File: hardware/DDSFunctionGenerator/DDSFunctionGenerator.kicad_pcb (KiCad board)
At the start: 2 copper layers, 100 x 100 mm, 147 parts, among them J1 Conn_Coaxial, J2 USB_B_Micro, J3 Conn_Coaxial, J4 Conn_Coaxial, Q1 Q_NPN_BEC, Q2 Q_NPN_BEC, Q3 Q_NPN_BEC, Q4 BC859, Q5 BC848, Q6 Q_NPN_BEC, SW1 Rotary_Encoder_Switch, T1 Transformer_1P_1S, U1 TC1107-3.3VOA, U10 74HCT1G86, U2 L7805, U3 L7805, U4 AD9832, U5 STM32F030K6Tx, U6 FT200XD, U7 AD8325, U8 MCP3425A0T-ECH, U9 LM358, X1 XO91, Y1 Crystal

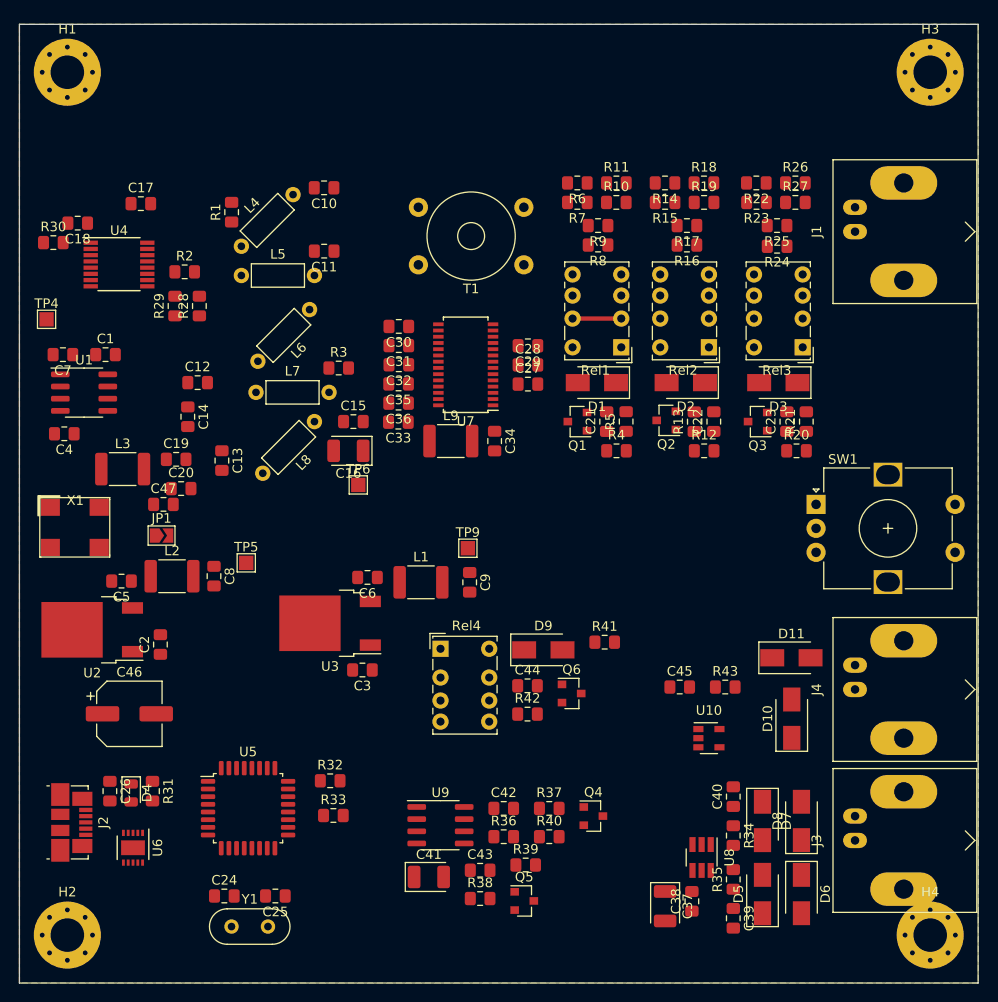
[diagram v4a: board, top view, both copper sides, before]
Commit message: added encoder 3d model
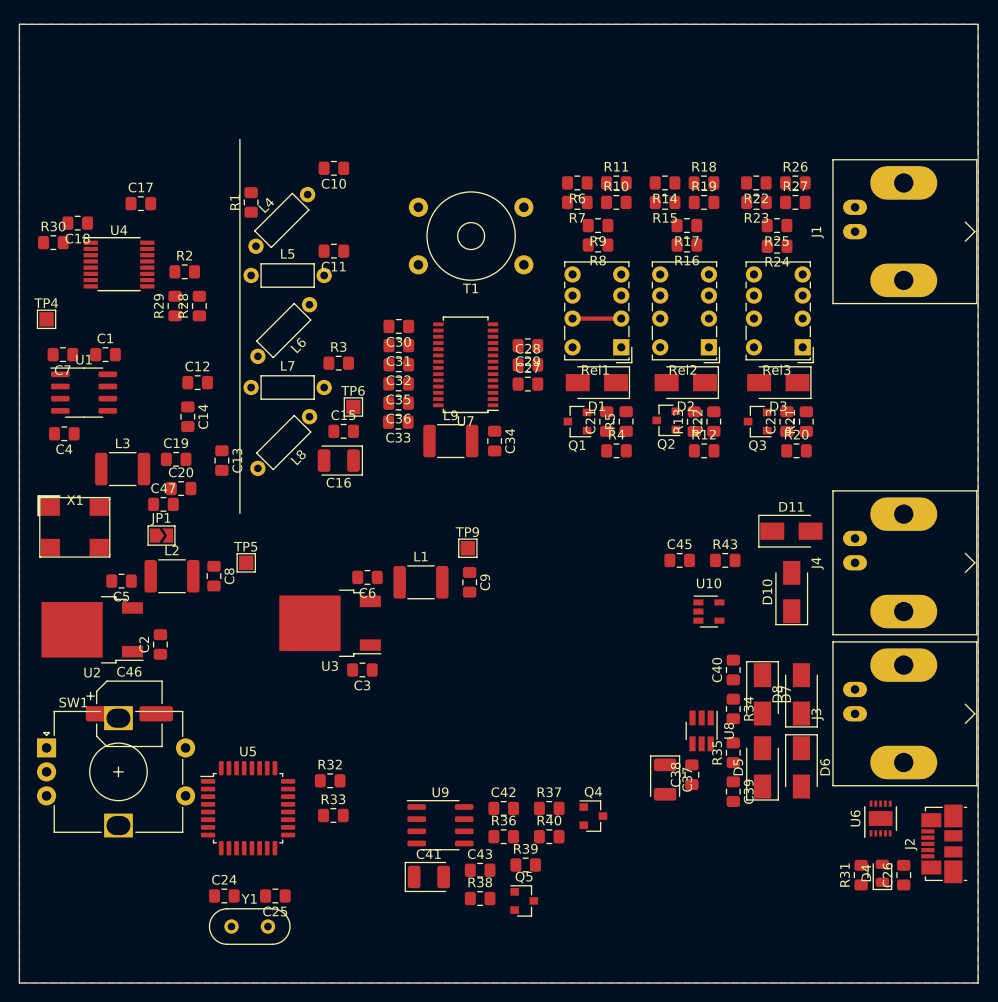
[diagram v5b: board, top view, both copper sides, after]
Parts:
- removed C44: 1n, Capacitor_SMD:C_0805_2012Metric_Pad1.15x1.40mm_HandSolder
- removed D9: D, Diode_SMD:D_SMA
- removed H1, H2, H3, H4: MountingHole_Pad, MountingHole:MountingHole_3.5mm_Pad_Via
- removed Q6: Q_NPN_BEC, Package_TO_SOT_SMD:SOT-23
- removed R41: 2k2, Resistor_SMD:R_0805_2012Metric_Pad1.15x1.40mm_HandSolder
- removed R42: 10k, Resistor_SMD:R_0805_2012Metric_Pad1.15x1.40mm_HandSolder
- removed Rel4: RSM850B-6112-85-1005, Relay_THT:Relay_DPDT_Omron_G6K-2P-Y
- moved J2 90.8 mm to (146.2, 135.5), turned to 90 degrees
- moved SW1 84.2 mm to (52.8, 125.5)
- moved C26 83.3 mm to (142.2, 138.7), turned to 90 degrees
- moved D4 78.8 mm to (140.0, 138.6), turned to 90 degrees
- moved U6 78.0 mm to (139.8, 132.8), turned to 90 degrees
- moved R31 74.4 mm to (137.8, 138.7), turned to 90 degrees
- moved C39 13.2 mm to (124.5, 130.0)
- moved C40 13.2 mm to (124.5, 117.3)
- moved D5 13.2 mm to (127.5, 127.5)
- moved D6 13.2 mm to (131.6, 127.5)
- moved R35 13.2 mm to (124.5, 126.0)
- moved U8 13.2 mm to (121.2, 123.7)
- moved C37 13.2 mm to (117.3, 128.8)
- moved C38 13.2 mm to (120.1, 128.3)
- moved C45 13.2 mm to (118.9, 105.9)
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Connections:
- R4 pad 2: REL_1 -> (no net)

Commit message: changed pcb size
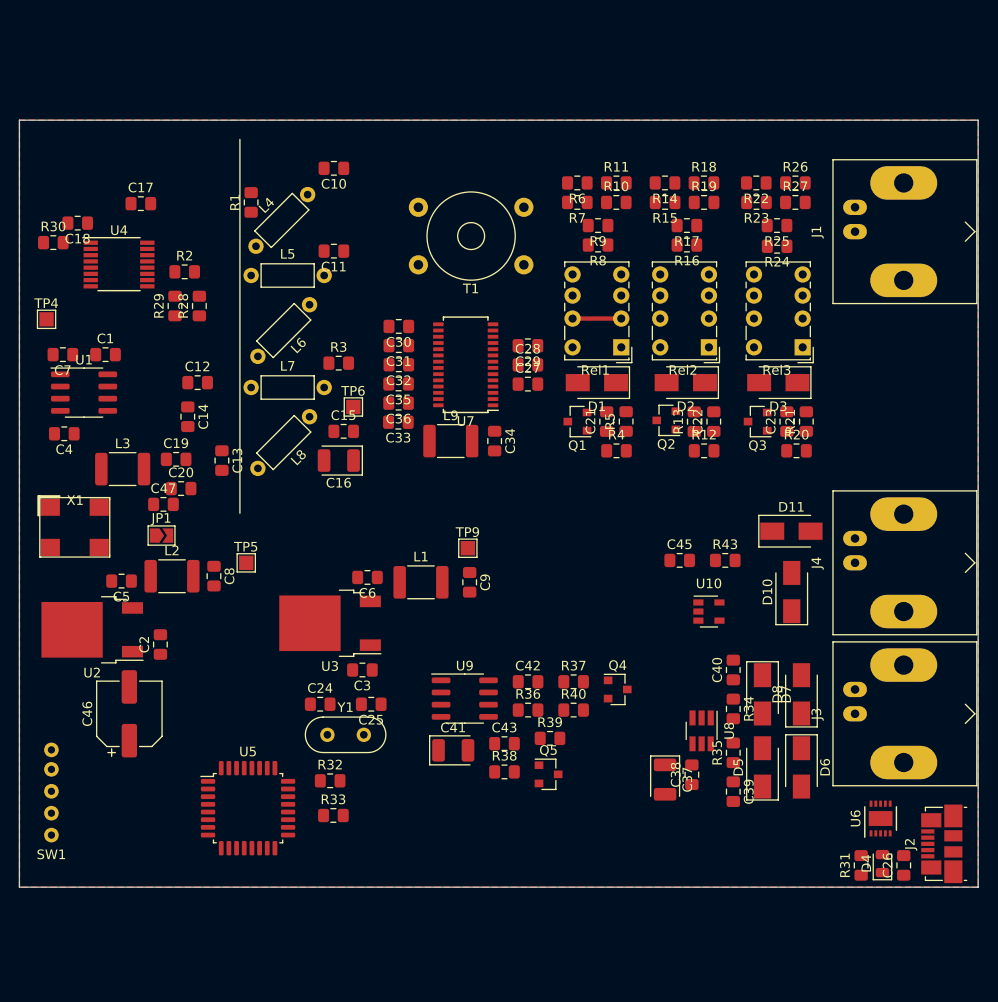
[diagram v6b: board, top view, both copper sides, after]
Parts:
- SW1: footprint Rotary_Encoder:RotaryEncoder_Alps_EC12E-Switch_Vertical_H20mm -> DDSFunctionGenerator:EN11-VNB1BQ15
- moved Y1 22.4 mm to (82.1, 124.1)
- moved C24 22.4 mm to (81.4, 120.9)
- moved C25 22.4 mm to (86.7, 120.9)
- moved C42 13.5 mm to (103.1, 118.6)
- moved R37 13.5 mm to (107.8, 118.6)
- moved U9 13.5 mm to (96.5, 120.3)
- moved Q4 13.5 mm to (112.4, 119.4)
- moved R36 13.5 mm to (103.1, 121.5)
- moved R40 13.5 mm to (107.8, 121.5)
- moved C43 13.5 mm to (100.6, 125.0)
- moved Q5 13.5 mm to (105.2, 128.2)
- moved C41 13.5 mm to (95.2, 125.7)
- moved R38 13.5 mm to (100.6, 128.0)
- moved R39 13.5 mm to (105.3, 124.5)
- moved SW1 11.6 mm to (53.3, 137.1), turned to 180 degrees
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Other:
- board size 100 x 100 mm -> 100 x 80 mm

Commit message: update to recent kicad version
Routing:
- net +9V: track 0.00 -> 11.7 mm
- net Net-(R14-Pad1): track 0.00 -> 10.4 mm
- net Net-(R24-Pad1): track 0.00 -> 10.3 mm
- net Net-(R6-Pad1): track 0.00 -> 10.3 mm
- net Net-(R10-Pad1): track 0.00 -> 10.2 mm
- net Net-(R16-Pad1): track 0.00 -> 10.2 mm
- net Net-(R22-Pad1): track 0.00 -> 10.2 mm
- net Net-(D1-Pad2): track 0.00 -> 8.40 mm
- net Net-(D2-Pad2): track 0.00 -> 8.32 mm
- net Net-(C23-Pad1): track 0.00 -> 6.14 mm
- net Net-(C21-Pad1): track 0.00 -> 6.14 mm
- net Net-(C22-Pad1): track 0.00 -> 6.06 mm
- net Net-(Rel3-Pad2): track 0.00 -> 5.08 mm
- net Net-(Rel2-Pad2): track 0.00 -> 5.08 mm
- net Net-(D3-Pad2): track 0.00 -> 3.91 mm
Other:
- net class Default: trace_width 0.25 -> 0.3048
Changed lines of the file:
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@@
-(kicad_pcb (version 20171130) (host pcbnew "(5.1.2)-1")
+(kicad_pcb (version 20171130) (host pcbnew 5.0.2-bee76a0~70~ubuntu18.04.1)
   (general
     (thickness 1.6)
     (drawings 5)
-    (tracks 1)
+    (tracks 76)
     (zones 0)
     (modules 137)
@@
   )
   (setup
-    (last_trace_width 0.25)
+    (last_trace_width 0.3048)
     (user_trace_width 0.4572)
     (trace_clearance 0.2)
@@
     (zone_45_only no)
     (trace_min 0.2)
+    (segment_width 0.2)
+    (edge_width 0.05)
     (via_size 0.8)
     (via_drill 0.4)
@@
     (uvia_min_size 0.2)
     (uvia_min_drill 0.1)
-    (edge_width 0.05)
-    (segment_width 0.2)
     (pcb_text_width 0.3)
     (pcb_text_size 1.5 1.5)
@@
   (net_class Default "This is the default net class."
     (clearance 0.2)
-    (trace_width 0.25)
+    (trace_width 0.3048)
     (via_dia 0.8)
     (via_drill 0.4)
@@
   (gr_line (start 150 60) (end 150 140) (layer Edge.Cuts) (width 0.05))
   (gr_line (start 50 60) (end 150 60) (layer Edge.Cuts) (width 0.05))
+  (segment (start 131.699 86.836) (end 131.159 87.376) (width 0.3048) (layer F.Cu) (net 1))
+  (segment (start 131.699 83.693) (end 131.699 86.836) (width 0.3048) (layer F.Cu) (net 1))
+  (segment (start 121.92 86.963) (end 121.507 87.376) (width 0.3048) (layer F.Cu) (net 1))
+  (segment (start 121.92 83.693) (end 121.92 86.963) (width 0.3048) (layer F.Cu) (net 1))
+  (segment (start 112.776 86.836) (end 112.236 87.376) (width 0.3048) (layer F.Cu) (net 1))
+  (segment (start 112.776 83.693) (end 112.776 86.836) (width 0.3048) (layer F.Cu) (net 1))
+  (segment (start 107.696 86.836) (end 108.236 87.376) (width 0.3048) (layer F.Cu) (net 3))
+  (segment (start 107.696 83.693) (end 107.696 86.836) (width 0.3048) (layer F.Cu) (net 3))
+  (segment (start 107.204 88.408) (end 108.236 87.376) (width 0.3048) (layer F.Cu) (net 3))
+  (segment (start 107.204 91.44) (end 107.204 88.408) (width 0.3048) (layer F.Cu) (net 3))
+  (segment (start 116.84 86.709) (end 117.507 87.376) (width 0.3048) (layer F.Cu) (net 4))
+  (segment (start 116.84 83.693) (end 116.84 86.709) (width 0.3048) (layer F.Cu) (net 4))
+  (segment (start 116.475 88.408) (end 117.507 87.376) (width 0.3048) (layer F.Cu) (net 4))
+  (segment (start 116.475 91.313) (end 116.475 88.408) (width 0.3048) (layer F.Cu) (net 4))
+  (segment (start 126.619 86.836) (end 127.159 87.376) (width 0.3048) (layer F.Cu) (net 6))
+  (segment (start 126.619 83.693) (end 126.619 86.836) (width 0.3048) (layer F.Cu) (net 6))
+  (segment (start 111.261 92.456) (end 111.252 92.465) (width 0.3048) (layer F.Cu) (net 26))
+  (segment (start 113.284 92.456) (end 111.261 92.456) (width 0.3048) (layer F.Cu) (net 26))
+  (segment (start 111.252 92.465) (end 111.252 94.488) (width 0.3048) (layer F.Cu) (net 26))
+  (segment (start 109.279 92.465) (end 109.204 92.39) (width 0.3048) (layer F.Cu) (net 26))
+  (segment (start 111.252 92.465) (end 109.279 92.465) (width 0.3048) (layer F.Cu) (net 26))
+  (segment (start 120.405 92.465) (end 120.396 92.474) (width 0.3048) (layer F.Cu) (net 27))
+  (segment (start 122.428 92.465) (end 120.405 92.465) (width 0.3048) (layer F.Cu) (net 27))
+  (segment (start 120.396 92.474) (end 120.396 94.488) (width 0.3048) (layer F.Cu) (net 27))
+  (segment (start 118.686 92.474) (end 118.475 92.263) (width 0.3048) (layer F.Cu) (net 27))
+  (segment (start 120.396 92.474) (end 118.686 92.474) (width 0.3048) (layer F.Cu) (net 27))
+  (segment (start 132.08 92.465) (end 130.048 92.465) (width 0.3048) (layer F.Cu) (net 28))
+  (segment (start 130.048 94.47) (end 130.03 94.488) (width 0.3048) (layer F.Cu) (net 28))
+  (segment (start 130.048 92.465) (end 130.048 94.47) (width 0.3048) (layer F.Cu) (net 28))
+  (segment (start 128.075 92.465) (end 128 92.39) (width 0.3048) (layer F.Cu) (net 28))
+  (segment (start 130.048 92.465) (end 128.075 92.465) (width 0.3048) (layer F.Cu) (net 28))
+  (segment (start 107.696 74.658) (end 107.696 76.093) (width 0.3048) (layer F.Cu) (net 29))
+  (segment (start 109.329 73.025) (end 107.696 74.658) (width 0.3048) (layer F.Cu) (net 29))
+  (segment (start 109.22 66.548) (end 109.22 68.58) (width 0.3048) (layer F.Cu) (net 29))
+  (segment (start 109.22 70.884) (end 109.329 70.993) (width 0.3048) (layer F.Cu) (net 29))
+  (segment (start 109.22 68.58) (end 109.22 70.884) (width 0.3048) (layer F.Cu) (net 29))
+  (segment (start 109.329 70.993) (end 109.329 73.025) (width 0.3048) (layer F.Cu) (net 29))
+  (segment (start 111.379 74.696) (end 112.776 76.093) (width 0.3048) (layer F.Cu) (net 30))
+  (segment (start 111.379 73.025) (end 111.379 74.696) (width 0.3048) (layer F.Cu) (net 30))
+  (segment (start 111.379 73.025) (end 111.379 70.993) (width 0.3048) (layer F.Cu) (net 30))
+  (segment (start 111.379 68.725) (end 111.234 68.58) (width 0.3048) (layer F.Cu) (net 30))
+  (segment (start 111.379 70.993) (end 111.379 68.725) (width 0.3048) (layer F.Cu) (net 30))
+  (segment (start 111.234 66.557) (end 111.243 66.548) (width 0.3048) (layer F.Cu) (net 30))
+  (segment (start 111.234 68.58) (end 111.234 66.557) (width 0.3048) (layer F.Cu) (net 30))
   (segment (start 107.823 80.693) (end 112.903 80.693) (width 0.4572) (layer F.Cu) (net 34))
+  (segment (start 118.6 73.025) (end 118.6 70.993) (width 0.3048) (layer F.Cu) (net 35))
+  (segment (start 118.6 68.807) (end 118.373 68.58) (width 0.3048) (layer F.Cu) (net 35))
+  (segment (start 118.6 70.993) (end 118.6 68.807) (width 0.3048) (layer F.Cu) (net 35))
+  (segment (start 118.373 66.557) (end 118.364 66.548) (width 0.3048) (layer F.Cu) (net 35))
+  (segment (start 118.373 68.58) (end 118.373 66.557) (width 0.3048) (layer F.Cu) (net 35))
+  (segment (start 118.6 74.333) (end 116.84 76.093) (width 0.3048) (layer F.Cu) (net 35))
+  (segment (start 118.6 73.025) (end 118.6 74.333) (width 0.3048) (layer F.Cu) (net 35))
+  (segment (start 120.65 73.025) (end 120.65 70.993) (width 0.3048) (layer F.Cu) (net 36))
+  (segment (start 120.65 68.843) (end 120.387 68.58) (width 0.3048) (layer F.Cu) (net 36))
+  (segment (start 120.65 70.993) (end 120.65 68.843) (width 0.3048) (layer F.Cu) (net 36))
+  (segment (start 120.387 66.557) (end 120.378 66.548) (width 0.3048) (layer F.Cu) (net 36))
+  (segment (start 120.387 68.58) (end 120.387 66.557) (width 0.3048) (layer F.Cu) (net 36))
+  (segment (start 120.65 74.823) (end 121.92 76.093) (width 0.3048) (layer F.Cu) (net 36))
+  (segment (start 120.65 73.025) (end 120.65 74.823) (width 0.3048) (layer F.Cu) (net 36))
+  (segment (start 116.84 80.693) (end 121.92 80.693) (width 0.3048) (layer F.Cu) (net 37))
+  (segment (start 128.007 74.705) (end 126.619 76.093) (width 0.3048) (layer F.Cu) (net 38))
+  (segment (start 128.007 73.152) (end 128.007 74.705) (width 0.3048) (layer F.Cu) (net 38))
+  (segment (start 128.007 71.002) (end 127.998 70.993) (width 0.3048) (layer F.Cu) (net 38))
+  (segment (start 128.007 73.152) (end 128.007 71.002) (width 0.3048) (layer F.Cu) (net 38))
+  (segment (start 127.998 68.671) (end 127.907 68.58) (width 0.3048) (layer F.Cu) (net 38))
+  (segment (start 127.998 70.993) (end 127.998 68.671) (width 0.3048) (layer F.Cu) (net 38))
+  (segment (start 127.907 66.566) (end 127.889 66.548) (width 0.3048) (layer F.Cu) (net 38))
+  (segment (start 127.907 68.58) (end 127.907 66.566) (width 0.3048) (layer F.Cu) (net 38))
+  (segment (start 130.057 74.451) (end 131.699 76.093) (width 0.3048) (layer F.Cu) (net 39))
+  (segment (start 130.057 73.152) (end 130.057 74.451) (width 0.3048) (layer F.Cu) (net 39))
+  (segment (start 130.057 71.002) (end 130.048 70.993) (width 0.3048) (layer F.Cu) (net 39))
+  (segment (start 130.057 73.152) (end 130.057 71.002) (width 0.3048) (layer F.Cu) (net 39))
+  (segment (start 130.048 68.716) (end 129.912 68.58) (width 0.3048) (layer F.Cu) (net 39))
+  (segment (start 130.048 70.993) (end 130.048 68.716) (width 0.3048) (layer F.Cu) (net 39))
+  (segment (start 129.912 68.58) (end 129.912 66.548) (width 0.3048) (layer F.Cu) (net 39))
+  (segment (start 126.619 80.693) (end 131.699 80.693) (width 0.3048) (layer F.Cu) (net 40))
   (zone (net 7) (net_name GND) (layer F.Cu) (hatch edge 0.508)
     (connect_pads (clearance 0.508))

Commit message: first routing
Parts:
- removed C41: CP, Capacitor_Tantalum_SMD:CP_EIA-3528-21_Kemet-B
- removed C42, C43: 100n, Capacitor_SMD:C_0805_2012Metric_Pad1.15x1.40mm_HandSolder
- removed Q4: BC859, Package_TO_SOT_SMD:SOT-23
- removed Q5: BC848, Package_TO_SOT_SMD:SOT-23
- removed R36, R37, R38, R39, R40: 49R9, Resistor_SMD:R_0805_2012Metric_Pad1.15x1.40mm_HandSolder
- removed U9: LM358, Package_SO:SOIC-8_3.9x4.9mm_P1.27mm
- moved JP1 25.4 mm to (53.1, 80.8), turned to 90 degrees
- moved X1 17.7 mm to (54.9, 82.0), turned to 90 degrees
- moved R30 9.42 mm to (62.5, 69.8), turned to 90 degrees
- moved TP4 9.40 mm to (62.2, 81.0)
- moved R29 5.94 mm to (72.1, 78.7), turned to 180 degrees
- moved R28 5.79 mm to (72.1, 74.7), turned to 180 degrees
- moved R26 5.59 mm to (125.3, 66.5), turned to 180 degrees
- moved R27 5.59 mm to (125.3, 68.6), turned to 180 degrees
- moved C17 5.12 mm to (67.3, 70.9)
- moved Q1 5.08 mm to (113.3, 91.4), turned to 90 degrees
- moved R20 5.08 mm to (126.0, 94.5), turned to 180 degrees
- moved R21 5.08 mm to (127.0, 91.4)
- moved R6 5.08 mm to (113.3, 66.5), turned to 0 degrees
- moved R7 5.08 mm to (113.3, 68.6), turned to 0 degrees
- moved C23 5.08 mm to (125.0, 91.4)
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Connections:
- net Net-(C47-Pad2) renamed /DDSSynthesizer/MCLK
- J2 pad 2: (no net) -> Net-(J2-Pad2)
- J2 pad 3: (no net) -> Net-(J2-Pad3)
- J2 pad 4: (no net) -> Net-(J2-Pad4)
- Q3 pad 3: (no net) -> Net-(Q3-Pad3)
- R12 pad 2: (no net) -> REL_2
- R20 pad 2: (no net) -> REL_3
- R32 pad 1: (no net) -> Net-(R32-Pad1)
- R32 pad 2: (no net) -> Net-(R32-Pad2)
- R33 pad 1: (no net) -> Net-(R33-Pad1)
- R33 pad 2: (no net) -> Net-(R33-Pad2)
- R4 pad 2: (no net) -> REL_1
- Rel1 pad 1: +9V -> Net-(D1-Pad2)
- Rel1 pad 3: RF_FROM_AMPLIFIER -> Net-(Rel1-Pad3)
- Rel1 pad 4: Net-(R10-Pad1) -> Net-(R6-Pad1)
- Rel1 pad 5: Net-(R6-Pad1) -> Net-(R10-Pad1)
- Rel1 pad 6: Net-(Rel1-Pad6) -> RF_FROM_AMPLIFIER
- Rel1 pad 8: Net-(D1-Pad2) -> +9V
- Rel2 pad 1: +9V -> Net-(D2-Pad2)
- Rel2 pad 3: Net-(Rel1-Pad6) -> Net-(Rel2-Pad3)
- Rel2 pad 4: Net-(R16-Pad1) -> Net-(R14-Pad1)
- Rel2 pad 5: Net-(R14-Pad1) -> Net-(R16-Pad1)
- Rel2 pad 6: Net-(Rel2-Pad6) -> Net-(Rel1-Pad3)
- Rel2 pad 8: Net-(D2-Pad2) -> +9V
- Rel3 pad 1: +9V -> Net-(D3-Pad2)
- Rel3 pad 3: Net-(Rel2-Pad6) -> Net-(J1-Pad1)
- Rel3 pad 4: Net-(R24-Pad1) -> Net-(R22-Pad1)
- Rel3 pad 5: Net-(R22-Pad1) -> Net-(R24-Pad1)
- Rel3 pad 6: Net-(J1-Pad1) -> Net-(Rel2-Pad3)
- Rel3 pad 8: Net-(D3-Pad2) -> +9V
- U1 pad 3: (no net) -> Net-(U1-Pad3)
- U1 pad 6: (no net) -> Net-(U1-Pad6)
- U1 pad 7: (no net) -> Net-(U1-Pad7)
- U10 pad 1: (no net) -> DIGITAL_OUTT_1
- U4 pad 2: (no net) -> Net-(U4-Pad2)
- U4 pad 3: (no net) -> Net-(U4-Pad3)
- U4 pad 7: (no net) -> SCLK
- U4 pad 9: (no net) -> FSYNC
- U5 pad 1: (no net) -> Net-(U5-Pad1)
- U5 pad 10: (no net) -> Net-(U5-Pad10)
- U5 pad 11: (no net) -> Net-(U5-Pad11)
- U5 pad 12: (no net) -> Net-(U5-Pad12)
- U5 pad 13: (no net) -> Net-(U5-Pad13)
- U5 pad 14: (no net) -> Net-(U5-Pad14)
- U5 pad 15: (no net) -> Net-(U5-Pad15)
- U5 pad 16: (no net) -> Net-(U5-Pad16)
- U5 pad 17: (no net) -> Net-(U5-Pad17)
- U5 pad 18: (no net) -> Net-(U5-Pad18)
- U5 pad 19: (no net) -> Net-(U5-Pad19)
- U5 pad 2: (no net) -> Net-(U5-Pad2)
- U5 pad 20: (no net) -> Net-(U5-Pad20)
- U5 pad 21: (no net) -> Net-(U5-Pad21)
- U5 pad 22: (no net) -> Net-(U5-Pad22)
- U5 pad 23: (no net) -> Net-(U5-Pad23)
- U5 pad 24: (no net) -> Net-(U5-Pad24)
- U5 pad 25: (no net) -> Net-(U5-Pad25)
- U5 pad 26: (no net) -> Net-(U5-Pad26)
- U5 pad 27: (no net) -> Net-(U5-Pad27)
- U5 pad 28: (no net) -> Net-(U5-Pad28)
- U5 pad 29: (no net) -> Net-(U5-Pad29)
- U5 pad 3: (no net) -> Net-(U5-Pad3)
- U5 pad 30: (no net) -> Net-(U5-Pad30)
- U5 pad 31: (no net) -> Net-(U5-Pad31)
- U5 pad 32: (no net) -> Net-(U5-Pad32)
- U5 pad 4: (no net) -> Net-(U5-Pad4)
- U5 pad 5: (no net) -> Net-(U5-Pad5)
- U5 pad 6: (no net) -> Net-(U5-Pad6)
- U5 pad 7: (no net) -> Net-(U5-Pad7)
- U5 pad 8: (no net) -> Net-(U5-Pad8)
- U5 pad 9: (no net) -> Net-(U5-Pad9)
- U6 pad 1: (no net) -> Net-(U6-Pad1)
- U6 pad 10: (no net) -> Net-(U6-Pad10)
- U6 pad 11: (no net) -> Net-(U6-Pad11)
- U6 pad 2: (no net) -> Net-(U6-Pad2)
- U6 pad 3: (no net) -> Net-(U6-Pad3)
- U6 pad 4: (no net) -> Net-(U6-Pad4)
- U6 pad 5: (no net) -> Net-(U6-Pad5)
- U6 pad 6: (no net) -> Net-(U6-Pad6)
- U6 pad 7: (no net) -> Net-(U6-Pad7)
- U6 pad 8: (no net) -> Net-(U6-Pad8)
- U6 pad 9: (no net) -> Net-(U6-Pad9)
- U7 pad 1: (no net) -> DATAEN
- U7 pad 25: (no net) -> Net-(U7-Pad25)
- U7 pad 3: (no net) -> CLK
- U7 pad 6: (no net) -> TXEN
- U7 pad 7: (no net) -> SLEEP
- U8 pad 3: (no net) -> SCL
- U8 pad 4: (no net) -> SDA
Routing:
- net Net-(C27-Pad1): track 0.00 -> 24.1 mm
- net Net-(L4-Pad1): track 0.00 -> 16.0 mm
- net Net-(C13-Pad2): track 0.00 -> 13.1 mm
- net RF_DDS: track 0.00 -> 12.6 mm
- net SLEEP: track 0.00 -> 9.18 mm
- net PSEL0: track 0.00 -> 8.32 mm
- net PSEL1: track 0.00 -> 7.61 mm
- net FSELECT: track 0.00 -> 7.48 mm
- net TXEN: track 0.00 -> 7.29 mm
- net SDATA: track 0.00 -> 6.99 mm
- net Net-(C11-Pad2): track 0.00 -> 6.22 mm
- net CLK: track 0.00 -> 4.92 mm
- net SCLK: track 0.00 -> 4.11 mm
- net Net-(C18-Pad1): track 0.00 -> 3.80 mm
- net Net-(C12-Pad2): track 0.00 -> 3.54 mm
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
